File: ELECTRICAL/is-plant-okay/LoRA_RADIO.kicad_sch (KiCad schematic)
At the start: 1 part, among them U9 Value

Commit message: feat: add pins for mcu
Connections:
- net MISO renamed LORA_MISO
- net MOSI renamed LORA_MOSI
- net SCLK renamed LORA_SCLK
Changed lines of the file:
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@@
 	)
 	(hierarchical_label "3.3V"
-		(shape output)
+		(shape input)
 		(at 118.11 87.63 180)
 		(effects
@@
 		)
 	)
-	(hierarchical_label "SCLK"
+	(hierarchical_label "LORA_SCLK"
 		(shape input)
 		(at 113.03 77.47 180)
@@
 		)
 	)
-	(hierarchical_label "MISO"
+	(hierarchical_label "LORA_MISO"
 		(shape output)
 		(at 113.03 72.39 180)
@@
 		)
 	)
-	(hierarchical_label "MOSI"
+	(hierarchical_label "LORA_MOSI"
 		(shape input)
 		(at 113.03 74.93 180)

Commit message: feat: add pins for bootloader programmer
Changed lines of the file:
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@@
 	)
 	(hierarchical_label "LORA_RST"
-		(shape input)
+		(shape output)
 		(at 113.03 80.01 180)
 		(effects

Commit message: feat: finished schematics
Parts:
- added SW1: LORA_RST, symbol Switch:SW_Push
- added TP7: LORA_3.3V_TP, TestPoint:TestPoint_Keystone_5000-5004_Miniature, symbol Connector:TestPoint
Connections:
- net 3.3V: now also TP7.1
- net GND: now also SW1.1
- net LORA_RST: no longer names the net of U9.5 (RST)
- net LORA_RST: now also SW1.2

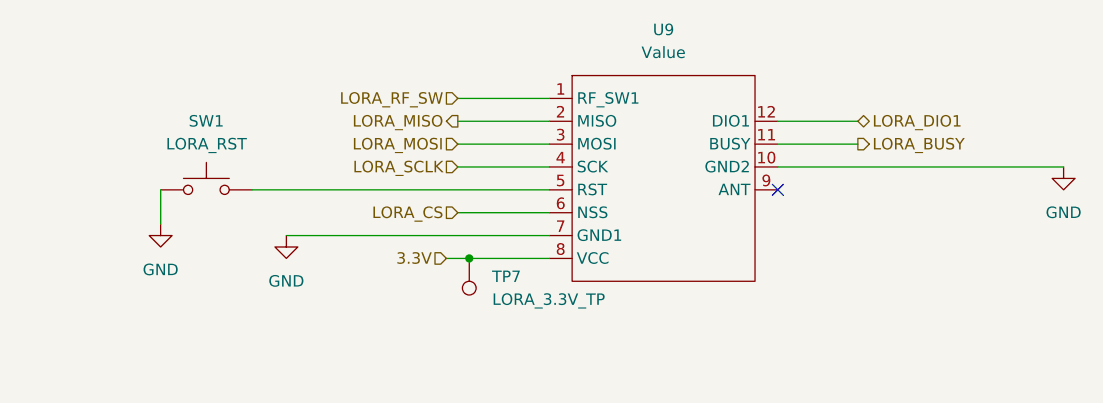
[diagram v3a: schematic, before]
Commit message: feat: add resistor footprint
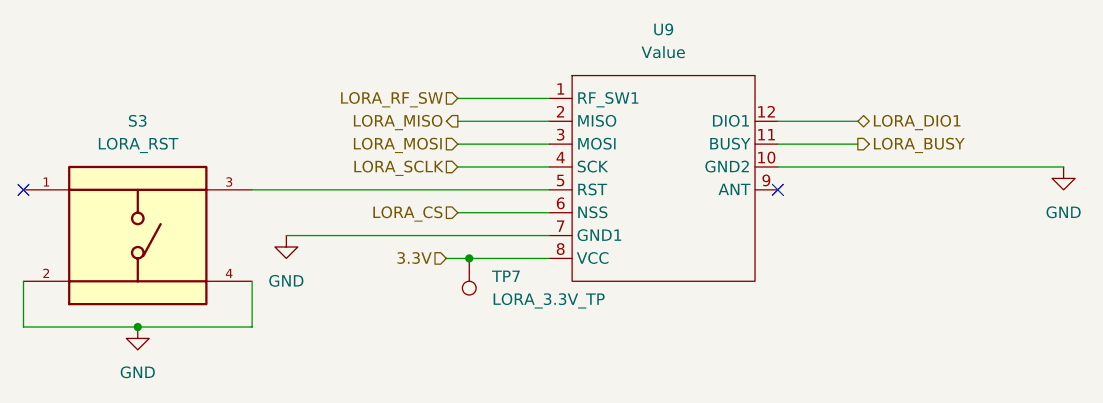
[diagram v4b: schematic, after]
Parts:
- removed SW1: LORA_RST, symbol Switch:SW_Push
- added S3: LORA_RST, is-plant-okay-foot:SW_TS04-66-55-BK-260-SMT, symbol is-plant-okay-lib:TS04-66-55-BK-260-SMT
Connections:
- net GND: now also S3.2, S3.4
- net at U9.5 (RST): now also S3.3
- no-connect marks 1 -> 2
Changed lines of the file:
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@@
 	(paper "A4")
+	(junction
+		(at 77.47 95.25)
+		(diameter 0)
+		(color 0 0 0 0)
+	)
 	(junction
 		(at 114.3 87.63)
@@
 	)
 	(no_connect
+		(at 64.77 80.01)
+	)
+	(no_connect
 		(at 148.59 80.01)
 	)
@@
 	(wire
 		(pts
+			(xy 64.77 90.17) (xy 64.77 95.25)
+		)
+		(stroke
+			(width 0)
+			(type default)
+		)
+	)
+	(wire
+		(pts
 			(xy 113.03 69.85) (xy 123.19 69.85)
 		)
@@
 	(wire
 		(pts
+			(xy 64.77 95.25) (xy 77.47 95.25)
+		)
+		(stroke
+			(width 0)
+			(type default)
+		)
+	)
+	(wire
+		(pts
 			(xy 148.59 74.93) (xy 157.48 74.93)
 		)
@@
 	(wire
 		(pts
-			(xy 80.01 80.01) (xy 80.01 83.82)
-		)
-		(stroke
-			(width 0)
-			(type default)
-		)
-	)
-	(wire
-		(pts
 			(xy 90.17 80.01) (xy 123.19 80.01)
 		)
@@
 	(wire
 		(pts
+			(xy 90.17 90.17) (xy 90.17 95.25)
+		)
+		(stroke
+			(width 0)
+			(type default)
+		)
+	)
+	(wire
+		(pts
 			(xy 148.59 77.47) (xy 180.34 77.47)
 		)
@@
 		(pts
 			(xy 114.3 87.63) (xy 123.19 87.63)
+		)
+		(stroke
+			(width 0)
+			(type default)
+		)
+	)
+	(wire
+		(pts
+			(xy 77.47 95.25) (xy 90.17 95.25)
 		)
 		(stroke
@@
 			)
 			(justify right)
-		)
-	)
-	(symbol
-		(lib_id "power:GND")
-		(at 80.01 83.82 0)
-		(unit 1)
-		(exclude_from_sim no)
-		(in_bom yes)
-		(on_board yes)
-		(dnp no)
-		(fields_autoplaced yes)
-		(property "Reference" "#PWR05"
-			(at 80.01 90.17 0)
-			(effects
-				(font
-					(size 1.27 1.27)
-				)
-				(hide yes)
-			)
-		)
-		(property "Value" "GND"
-			(at 80.01 88.9 0)
-			(effects
-				(font
-					(size 1.27 1.27)
-				)
-			)
-		)
-		(property "Footprint" ""
-			(at 80.01 83.82 0)
-			(effects
-				(font
-					(size 1.27 1.27)
-				)
-				(hide yes)
-			)
-		)
-		(property "Datasheet" ""
-			(at 80.01 83.82 0)
-			(effects
-				(font
-					(size 1.27 1.27)
-				)
-				(hide yes)
-			)
-		)
-		(property "Description" "Power symbol creates a global label with name \"GND\" , ground"
-			(at 80.01 83.82 0)
-			(effects
-				(font
-					(size 1.27 1.27)
-				)
-				(hide yes)
-			)
-		)
-		(pin "1"
-		)
-		(instances
-			(project "is-plant-okay"
-				(path "/ac51c2f9-77a4-4b89-b63f-6e0ba02b1e45/08e21840-3bd7-4f63-bbb0-33a00ebd42b3"
-					(reference "#PWR05")
-					(unit 1)
-				)
-			)
 		)
 	)
@@
 	)
 	(symbol
+		(lib_id "is-plant-okay-lib:TS04-66-55-BK-260-SMT")
+		(at 77.47 85.09 0)
+		(unit 1)
+		(exclude_from_sim no)
+		(in_bom yes)
+		(on_board yes)
+		(dnp no)
+		(fields_autoplaced yes)
+		(property "Reference" "S3"
+			(at 77.47 72.39 0)
+			(effects
+				(font
+					(size 1.27 1.27)
+				)
+			)
+		)
+		(property "Value" "LORA_RST"
+			(at 77.47 74.93 0)
+			(effects
+				(font
+					(size 1.27 1.27)
+				)
+			)
+		)
+		(property "Footprint" "is-plant-okay-foot:SW_TS04-66-55-BK-260-SMT"
+			(at 77.47 85.09 0)
+			(effects
+				(font
+					(size 1.27 1.27)
+				)
+				(justify bottom)
+				(hide yes)
+			)
+		)
+		(property "Datasheet" "https://www.sameskydevices.com/product/resource/ts04.pdf"
+			(at 77.47 85.09 0)
+			(effects
+				(font
+					(size 1.27 1.27)
+				)
+				(hide yes)
+			)
+		)
+		(property "Description" "SWITCH TACTILE SPST-NO 0.05A 12V"
+			(at 77.47 85.09 0)
+			(effects
+				(font
+					(size 1.27 1.27)
+				)
+				(hide yes)
+			)
+		)
+		(property "MANUFACTURER" "CUI Devices"
+			(at 77.47 85.09 0)
+			(effects
+				(font
+					(size 1.27 1.27)
+				)
+				(justify bottom)
+				(hide yes)
+			)
+		)
+		(property "MFG PART #" "TS04-66-55-BK-260-SMT"
+			(at 77.47 85.09 0)
+			(effects
+				(font
+					(size 1.27 1.27)
+				)
+				(hide yes)
+			)
+		)
+		(property "TYPE" "SMD"
+			(at 77.47 85.09 0)
+			(effects
+				(font
+					(size 1.27 1.27)
+				)
+				(hide yes)
+			)
+		)
+		(property "PACKAGE" "~"
+			(at 77.47 85.09 0)
+			(effects
+				(font
+					(size 1.27 1.27)
+				)
+				(hide yes)
+			)
+		)
+		(pin "4"
+		)
+		(pin "3"
+		)
+		(pin "2"
+		)
+		(pin "1"
+		)
+		(instances
+			(project ""
+				(path "/ac51c2f9-77a4-4b89-b63f-6e0ba02b1e45/08e21840-3bd7-4f63-bbb0-33a00ebd42b3"
+					(reference "S3")
+					(unit 1)
+				)
+			)
+		)
+	)
+	(symbol
 		(lib_id "Connector:TestPoint")
 		(at 114.3 87.63 180)
@@
 	)
 	(symbol
-		(lib_id "Switch:SW_Push")
-		(at 85.09 80.01 0)
+		(lib_id "power:GND")
+		(at 77.47 95.25 0)
 		(unit 1)
 		(exclude_from_sim no)
@@
 		(dnp no)
 		(fields_autoplaced yes)
-		(property "Reference" "SW1"
-			(at 85.09 72.39 0)
-			(effects
-				(font
-					(size 1.27 1.27)
-				)
-			)
-		)
-		(property "Value" "LORA_RST"
-			(at 85.09 74.93 0)
+		(property "Reference" "#PWR05"
+			(at 77.47 101.6 0)
+			(effects
+				(font
+					(size 1.27 1.27)
+				)
+				(hide yes)
+			)
+		)
+		(property "Value" "GND"
+			(at 77.47 100.33 0)
 			(effects
 				(font
@@
 		)
 		(property "Footprint" ""
-			(at 85.09 74.93 0)
-			(effects
-				(font
-					(size 1.27 1.27)
-				)
-				(hide yes)
-			)
-		)
-		(property "Datasheet" "~"
-			(at 85.09 74.93 0)
-			(effects
-				(font
-					(size 1.27 1.27)
-				)
-				(hide yes)
-			)
-		)
-		(property "Description" "Push button switch, generic, two pins"
-			(at 85.09 80.01 0)
-			(effects
-				(font
-					(size 1.27 1.27)
-				)
-				(hide yes)
-			)
-		)
-		(pin "2"
+			(at 77.47 95.25 0)
+			(effects
+				(font
+					(size 1.27 1.27)
+				)
+				(hide yes)
+			)
+		)
+		(property "Datasheet" ""
+			(at 77.47 95.25 0)
+			(effects
+				(font
+					(size 1.27 1.27)
+				)
+				(hide yes)
+			)
+		)
+		(property "Description" "Power symbol creates a global label with name \"GND\" , ground"
+			(at 77.47 95.25 0)
+			(effects
+				(font
+					(size 1.27 1.27)
+				)
+				(hide yes)
+			)
 		)
 		(pin "1"
@@
 			(project "is-plant-okay"
 				(path "/ac51c2f9-77a4-4b89-b63f-6e0ba02b1e45/08e21840-3bd7-4f63-bbb0-33a00ebd42b3"
-					(reference "SW1")
+					(reference "#PWR05")
 					(unit 1)
 				)
